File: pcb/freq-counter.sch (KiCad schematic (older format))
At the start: 63 parts, among them J1 RPM on board, J11 Hz/RPM_Terminal1, J12 Hz/RPM_Terminal0, J13 1kMG_Terminal1, J14 1kMG_Terminal0, J2 BNC, J3 RPM to Board, J4 Jack-DC, J5 Segments-Terminal0, J6 Power-Digits_Terminal0, J7 Segments-Terminal1, J8 Power-Digits_Terminal1, J9 Power-Terminal1, Q1 CSC388A, Q2 CSC388A, Q3 2SA1015, Q4 2SC1815, Q5 2SC1815, SW1 on/off, SW2 count up, SW3 toggle, SW4 SW_SIGNAL, U1 SN74HC02N, U2 ATTINY4313-PU(freq-counter), U3 EE-SX460, Y1 10MHz

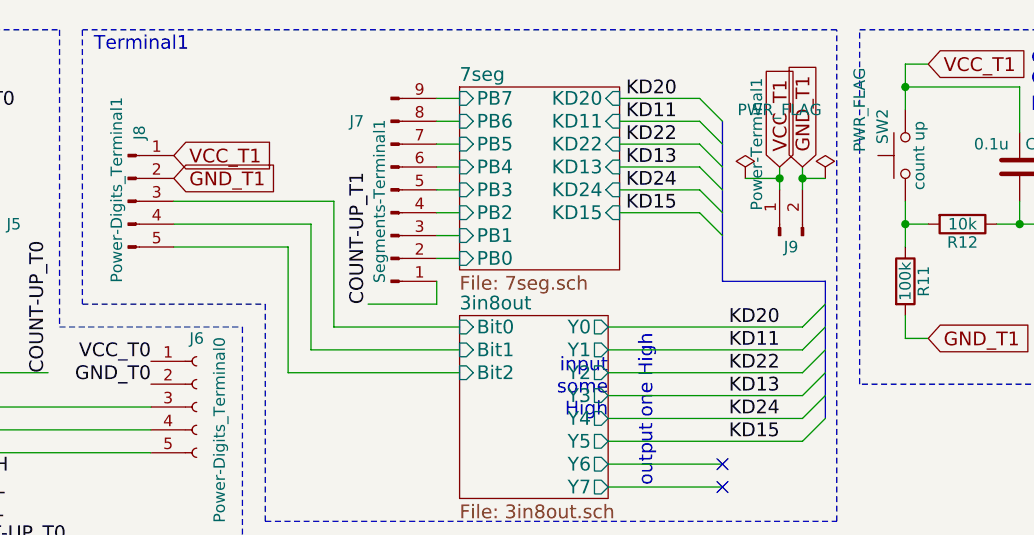
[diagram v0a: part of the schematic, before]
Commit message: ほぼ完成。電源ON/OFFの switch を slide switch に変更する必要があるけど保留。
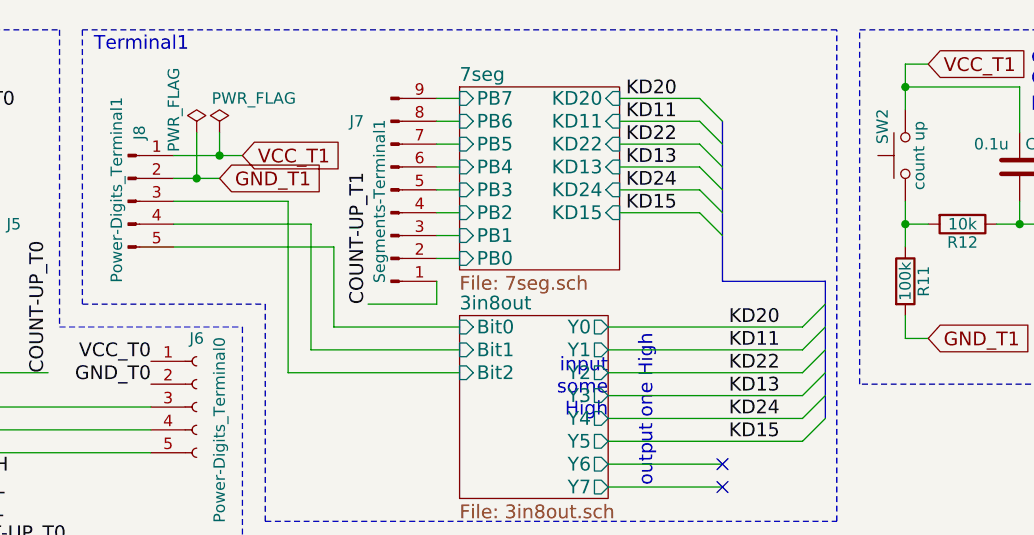
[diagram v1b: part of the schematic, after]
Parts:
- removed J9: Power-Terminal1, Conn_JST:JST_XH_B02B-XH-A_1x02_P2.50mm_Horizontal, symbol Conn_01x02_Male
- J1, J3: footprint Conn_JST:JST_XH_B03B-XH-A_1x03_P2.50mm_Horizontal -> Connector_JST:JST_XH_B03B-XH-A_1x03_P2.50mm_Horizontal
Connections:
- net 3in8out/Bit0: now also J8.5 (Pin_5); no longer J8.3 (Pin_3)
- net 3in8out/Bit2: now also J8.3 (Pin_3); no longer J8.5 (Pin_5)
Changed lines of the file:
@@
 $EndComp
 $Comp
-L GND #PWR4
+L GND #PWR01
 U 1 1 5A10C10B
 P 1450 5100
-F 0 "#PWR4" H 1450 4850 50  0001 C CNN
+F 0 "#PWR01" H 1450 4850 50  0001 C CNN
 F 1 "GND" H 1450 4950 50  0000 C CNN
 F 2 "" H 1450 5100 50  0001 C CNN
@@
 $EndComp
 $Comp
-L GND #PWR13
+L GND #PWR02
 U 1 1 5A102C86
 P 5050 6000
-F 0 "#PWR13" H 5050 5750 50  0001 C CNN
+F 0 "#PWR02" H 5050 5750 50  0001 C CNN
 F 1 "GND" H 5050 5850 50  0000 C CNN
 F 2 "" H 5050 6000 50  0001 C CNN
@@
 F 0 "J3" H 6850 5400 50  0000 C CNN
 F 1 "RPM to Board" H 6850 5000 50  0000 C CNN
-F 2 "Conn_JST:JST_XH_B03B-XH-A_1x03_P2.50mm_Horizontal" H 6850 5200 50  0001 C CNN
+F 2 "Connector_JST:JST_XH_B03B-XH-A_1x03_P2.50mm_Horizontal" H 6850 5200 50  0001 C CNN
 F 3 "" H 6850 5200 50  0001 C CNN
 	1    6850 5200
@@
 F 0 "J1" H 4750 4600 50  0000 C CNN
 F 1 "RPM on board" H 4650 4200 50  0000 C CNN
-F 2 "Conn_JST:JST_XH_B03B-XH-A_1x03_P2.50mm_Horizontal" H 4750 4400 50  0001 C CNN
+F 2 "Connector_JST:JST_XH_B03B-XH-A_1x03_P2.50mm_Horizontal" H 4750 4400 50  0001 C CNN
 F 3 "" H 4750 4400 50  0001 C CNN
 	1    4750 4400
@@
 $EndComp
 $Comp
-L GND #PWR3
+L GND #PWR03
 U 1 1 5A14ACE7
 P 1250 2200
-F 0 "#PWR3" H 1250 1950 50  0001 C CNN
+F 0 "#PWR03" H 1250 1950 50  0001 C CNN
 F 1 "GND" H 1250 2050 50  0000 C CNN
 F 2 "" H 1250 2200 50  0001 C CNN
@@
 $EndComp
 $Comp
-L PWR_FLAG #FLG1
+L PWR_FLAG #FLG04
 U 1 1 5A14B084
 P 1150 2000
-F 0 "#FLG1" H 1150 2075 50  0001 C CNN
+F 0 "#FLG04" H 1150 2075 50  0001 C CNN
 F 1 "PWR_FLAG" H 1150 2150 50  0000 C CNN
 F 2 "" H 1150 2000 50  0001 C CNN
@@
 $EndComp
 $Comp
-L PWR_FLAG #FLG2
+L PWR_FLAG #FLG05
 U 1 1 5A14B889
 P 1950 1050
-F 0 "#FLG2" H 1950 1125 50  0001 C CNN
+F 0 "#FLG05" H 1950 1125 50  0001 C CNN
 F 1 "PWR_FLAG" H 2100 1350 50  0000 C CNN
 F 2 "" H 1950 1050 50  0001 C CNN
@@
 $EndComp
 $Comp
-L GND #PWR8
+L GND #PWR06
 U 1 1 5A14CF4C
 P 2900 1700
-F 0 "#PWR8" H 2900 1450 50  0001 C CNN
+F 0 "#PWR06" H 2900 1450 50  0001 C CNN
 F 1 "GND" H 2900 1550 50  0000 C CNN
 F 2 "" H 2900 1700 50  0001 C CNN
@@
 Power
 $Comp
-L PWR_FLAG #FLG4
+L PWR_FLAG #FLG07
 U 1 1 5A15C58C
 P 5500 5050
-F 0 "#FLG4" H 5500 5125 50  0001 C CNN
+F 0 "#FLG07" H 5500 5125 50  0001 C CNN
 F 1 "PWR_FLAG" H 5450 5200 50  0000 C CNN
 F 2 "" H 5500 5050 50  0001 C CNN
@@
 $EndComp
 $Comp
-L PWR_FLAG #FLG3
+L PWR_FLAG #FLG08
 U 1 1 5A15C934
 P 5450 5400
-F 0 "#FLG3" H 5450 5475 50  0001 C CNN
+F 0 "#FLG08" H 5450 5475 50  0001 C CNN
 F 1 "PWR_FLAG" V 5350 5400 50  0000 C CNN
 F 2 "" H 5450 5400 50  0001 C CNN
@@
 NoConn ~ 1200 1150
 $Comp
-L VCC #PWR5
+L VCC #PWR09
 U 1 1 5A193502
 P 2050 1050
-F 0 "#PWR5" H 2050 900 50  0001 C CNN
+F 0 "#PWR09" H 2050 900 50  0001 C CNN
 F 1 "VCC" H 2050 1200 50  0000 C CNN
 F 2 "" H 2050 1050 50  0001 C CNN
@@
 Terminal1
 $Comp
-L Conn_01x02_Male J9
-U 1 1 5A1FF28B
-P 8800 1650
-F 0 "J9" V 8750 1600 50  0000 C CNN
-F 1 "Power-Terminal1" H 9200 1750 50  0000 C CNN
-F 2 "Conn_JST:JST_XH_B02B-XH-A_1x02_P2.50mm_Horizontal" H 8800 1650 50  0001 C CNN
-F 3 "" H 8800 1650 50  0001 C CNN
-	1    8800 1650
-	0    -1   -1   0
-$EndComp
-Text GLabel 8900 1350 1    60   Input ~ 0
-GND_T1
-$Comp
-L VCC #PWR7
+L VCC #PWR010
 U 1 1 5A20AA1B
 P 2800 1100
-F 0 "#PWR7" H 2800 950 50  0001 C CNN
+F 0 "#PWR010" H 2800 950 50  0001 C CNN
 F 1 "VCC" H 2800 1250 50  0000 C CNN
 F 2 "" H 2800 1100 50  0001 C CNN
@@
 	1    0    0    -1
 $EndComp
-Text GLabel 8800 1350 1    60   Input ~ 0
-VCC_T1
-$Comp
-L PWR_FLAG #FLG6
+$Comp
+L PWR_FLAG #FLG011
 U 1 1 5A1E7BBB
-P 9000 1400
-F 0 "#FLG6" H 9000 1475 50  0001 C CNN
-F 1 "PWR_FLAG" V 9150 1700 50  0000 C CNN
-F 2 "" H 9000 1400 50  0001 C CNN
-F 3 "" H 9000 1400 50  0001 C CNN
-	1    9000 1400
-	1    0    0    -1
-$EndComp
-$Comp
-L PWR_FLAG #FLG5
+P 6350 1200
+F 0 "#FLG011" H 6350 1275 50  0001 C CNN
+F 1 "PWR_FLAG" H 6500 1350 50  0000 C CNN
+F 2 "" H 6350 1200 50  0001 C CNN
+F 3 "" H 6350 1200 50  0001 C CNN
+	1    6350 1200
+	1    0    0    -1
+$EndComp
+$Comp
+L PWR_FLAG #FLG012
 U 1 1 5A1E8382
-P 8650 1400
-F 0 "#FLG5" H 8650 1475 50  0001 C CNN
-F 1 "PWR_FLAG" H 8800 1700 50  0000 C CNN
-F 2 "" H 8650 1400 50  0001 C CNN
-F 3 "" H 8650 1400 50  0001 C CNN
-	1    8650 1400
-	1    0    0    -1
-$EndComp
-$Comp
-L VCC #PWR2
+P 6250 1200
+F 0 "#FLG012" H 6250 1275 50  0001 C CNN
+F 1 "PWR_FLAG" V 6150 1300 50  0000 C CNN
+F 2 "" H 6250 1200 50  0001 C CNN
+F 3 "" H 6250 1200 50  0001 C CNN
+	1    6250 1200
+	1    0    0    -1
+$EndComp
+$Comp
+L VCC #PWR013
 U 1 1 5A1EAB1C
 P 1000 4500
-F 0 "#PWR2" H 1000 4350 50  0001 C CNN
+F 0 "#PWR013" H 1000 4350 50  0001 C CNN
 F 1 "VCC" H 1000 4650 50  0000 C CNN
 F 2 "" H 1000 4500 50  0001 C CNN
@@
 $EndComp
 $Comp
-L GND #PWR11
+L GND #PWR014
 U 1 1 5A1EBF20
 P 3100 3100
-F 0 "#PWR11" H 3100 2850 50  0001 C CNN
+F 0 "#PWR014" H 3100 2850 50  0001 C CNN
 F 1 "GND" H 3100 2950 50  0000 C CNN
 F 2 "" H 3100 3100 50  0001 C CNN
@@
 $EndComp
 $Comp
-L GND #PWR6
+L GND #PWR015
 U 1 1 5A1ECBC1
 P 2450 6400
-F 0 "#PWR6" H 2450 6150 50  0001 C CNN
+F 0 "#PWR015" H 2450 6150 50  0001 C CNN
 F 1 "GND" H 2450 6250 50  0000 C CNN
 F 2 "" H 2450 6400 50  0001 C CNN
@@
 $EndComp
 $Comp
-L GND #PWR1
+L GND #PWR016
 U 1 1 5A1ED93F
 P 850 4550
-F 0 "#PWR1" H 850 4300 50  0001 C CNN
+F 0 "#PWR016" H 850 4300 50  0001 C CNN
 F 1 "GND" H 850 4400 50  0000 C CNN
 F 2 "" H 850 4550 50  0001 C CNN
@@
 $EndComp
 $Comp
-L GND #PWR10
+L GND #PWR017
 U 1 1 5A1EE509
 P 2950 4800
-F 0 "#PWR10" H 2950 4550 50  0001 C CNN
+F 0 "#PWR017" H 2950 4550 50  0001 C CNN
 F 1 "GND" H 2950 4650 50  0000 C CNN
 F 2 "" H 2950 4800 50  0001 C CNN
@@
 $EndComp
 $Comp
-L VCC #PWR12
+L VCC #PWR018
 U 1 1 5A1EEDD1
 P 3100 5250
-F 0 "#PWR12" H 3100 5100 50  0001 C CNN
+F 0 "#PWR018" H 3100 5100 50  0001 C CNN
 F 1 "VCC" H 3100 5400 50  0000 C CNN
 F 2 "" H 3100 5250 50  0001 C CNN
@@
 $EndComp
 $Comp
-L VCC #PWR9
+L VCC #PWR019
 U 1 1 5A1EFB20
 P 2950 3700
-F 0 "#PWR9" H 2950 3550 50  0001 C CNN
+F 0 "#PWR019" H 2950 3550 50  0001 C CNN
 F 1 "VCC" H 2950 3850 50  0000 C CNN
 F 2 "" H 2950 3700 50  0001 C CNN
@@
 $EndComp
 $Comp
-L GND #PWR17
+L GND #PWR020
 U 1 1 5A1F0879
 P 7900 6150
-F 0 "#PWR17" H 7900 5900 50  0001 C CNN
+F 0 "#PWR020" H 7900 5900 50  0001 C CNN
 F 1 "GND" H 7900 6000 50  0000 C CNN
 F 2 "" H 7900 6150 50  0001 C CNN
@@
 $EndComp
 $Comp
-L VCC #PWR16
+L VCC #PWR021
 U 1 1 5A1F0C13
 P 7900 3850
-F 0 "#PWR16" H 7900 3700 50  0001 C CNN
+F 0 "#PWR021" H 7900 3700 50  0001 C CNN
 F 1 "VCC" H 7900 4000 50  0000 C CNN
 F 2 "" H 7900 3850 50  0001 C CNN
@@
 $EndComp
 $Comp
-L GND #PWR15
+L GND #PWR022
 U 1 1 5A1F3CDE
 P 6350 3650
-F 0 "#PWR15" H 6350 3400 50  0001 C CNN
+F 0 "#PWR022" H 6350 3400 50  0001 C CNN
 F 1 "GND" H 6350 3500 50  0000 C CNN
 F 2 "" H 6350 3650 50  0001 C CNN
@@
 $EndComp
 $Comp
-L VCC #PWR14
+L VCC #PWR023
 U 1 1 5A1F4C25
 P 5800 4400
-F 0 "#PWR14" H 5800 4250 50  0001 C CNN
+F 0 "#PWR023" H 5800 4250 50  0001 C CNN
 F 1 "VCC" H 5800 4550 50  0000 C CNN
 F 2 "" H 5800 4400 50  0001 C CNN
@@
 	5000 2700 5100 2700
 Wire Wire Line
-	6650 2250 7400 2250
-Wire Wire Line
-	6850 2050 7400 2050
-Wire Wire Line
-	6750 2150 7400 2150
-Wire Wire Line
 	7300 1750 7400 1750
 Wire Wire Line
@@
 	9050 750  5750 750
 Wire Wire Line
-	8800 1350 8800 1450
-Wire Wire Line
-	8900 1350 8900 1450
-Wire Wire Line
 	2050 1500 2000 1500
 Wire Wire Line
@@
 Wire Wire Line
 	1850 1150 2050 1150
-Wire Wire Line
-	9000 1400 8900 1400
-Connection ~ 8900 1400
-Wire Wire Line
-	8650 1400 8800 1400
-Connection ~ 8800 1400
 Wire Wire Line
 	3100 3100 3100 3000
@@
 	1    0    0    -1
 $EndComp
-Text GLabel 6150 1300 2    60   Input ~ 0
+Text GLabel 6450 1300 2    60   Input ~ 0
 VCC_T1
-Text GLabel 6150 1400 2    60   Input ~ 0
+Text GLabel 6350 1400 2    60   Input ~ 0
 GND_T1
 Wire Wire Line
-	6150 1500 6850 1500
-Wire Wire Line
-	6850 1500 6850 2050
+	6150 1500 6650 1500
+Wire Wire Line
+	6650 1500 6650 2250
 Wire Wire Line
 	6150 1600 6750 1600
@@
 	6750 1600 6750 2150
 Wire Wire Line
-	6650 2250 6650 1700
-Wire Wire Line
-	6650 1700 6150 1700
+	6850 1700 6150 1700
 Wire Notes Line
 	5750 750  5750 1950
@@
 Wire Notes Line
 	6550 1950 6550 2900
+Wire Wire Line
+	6750 2150 7400 2150
+Wire Wire Line
+	6650 2250 7400 2250
+Wire Wire Line
+	6850 1700 6850 2050
+Wire Wire Line
+	6850 2050 7400 2050
+Wire Wire Line
+	6350 1400 6150 1400
+Wire Wire Line
+	6150 1300 6450 1300
+Wire Wire Line
+	6250 1200 6250 1400
+Connection ~ 6250 1400
+Wire Wire Line
+	6350 1200 6350 1300
+Connection ~ 6350 1300
 $EndSCHEMATC

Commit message: Power ON/OFF switch を slide switch に変更。
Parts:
- SW1: footprint freq-counter:SW_Toggle_x1 -> freq-counter:SS12D01G4
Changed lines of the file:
@@
 F 0 "SW1" H 1650 1420 50  0000 C CNN
 F 1 "on/off" H 1650 1500 50  0000 C CNN
-F 2 "freq-counter:SW_Toggle_x1" H 1650 1250 50  0001 C CNN
+F 2 "freq-counter:SS12D01G4" H 1650 1250 50  0001 C CNN
 F 3 "" H 1650 1250 50  0001 C CNN
 	1    1650 1250

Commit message: RPM on board を PinHeaderに変更。
手持ちの部品にJST_XH_B03B-XH-A_1x03_P2.50mmの横向きがなかったため。
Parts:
- J1: footprint Connector_JST:JST_XH_B03B-XH-A_1x03_P2.50mm_Horizontal -> Connector_PinHeader_2.54mm:PinHeader_1x03_P2.54mm_Horizontal
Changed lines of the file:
@@
 F 0 "J1" H 4750 4600 50  0000 C CNN
 F 1 "RPM on board" H 4650 4200 50  0000 C CNN
-F 2 "Connector_JST:JST_XH_B03B-XH-A_1x03_P2.50mm_Horizontal" H 4750 4400 50  0001 C CNN
+F 2 "Connector_PinHeader_2.54mm:PinHeader_1x03_P2.54mm_Horizontal" H 4750 4400 50  0001 C CNN
 F 3 "" H 4750 4400 50  0001 C CNN
 	1    4750 4400

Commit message: ON/OFF の slide switch を横型に変更。
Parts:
- SW1: footprint freq-counter:SS12D01G4 -> freq-counter:SK-12D01-VG4
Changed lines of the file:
@@
 F 0 "SW1" H 1650 1420 50  0000 C CNN
 F 1 "on/off" H 1650 1500 50  0000 C CNN
-F 2 "freq-counter:SS12D01G4" H 1650 1250 50  0001 C CNN
+F 2 "freq-counter:SK-12D01-VG4" H 1650 1250 50  0001 C CNN
 F 3 "" H 1650 1250 50  0001 C CNN
 	1    1650 1250

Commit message: Power ON/OFF の slide switch を横型から縦型に変更。
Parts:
- SW1: footprint freq-counter:SK-12D01-VG4 -> freq-counter:SS12D01G4
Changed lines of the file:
@@
 F 0 "SW1" H 1650 1420 50  0000 C CNN
 F 1 "on/off" H 1650 1500 50  0000 C CNN
-F 2 "freq-counter:SK-12D01-VG4" H 1650 1250 50  0001 C CNN
+F 2 "freq-counter:SS12D01G4" H 1650 1250 50  0001 C CNN
 F 3 "" H 1650 1250 50  0001 C CNN
 	1    1650 1250

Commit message: 3Dpackages が表示されるように，旧式の3D modelを使うようにした。
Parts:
- C1, C3, C7: footprint Capacitors_THT:CP_Radial_D5.0mm_P2.50mm -> Capacitor_THT:CP_Radial_D5.0mm_P2.50mm
- C2, C4, C8, C9: footprint Capacitors_THT:C_Disc_D3.4mm_W2.1mm_P2.50mm -> Capacitor_THT:C_Disc_D3.0mm_W1.6mm_P2.50mm
- C5, C6: footprint Capacitors_THT:C_Disc_D3.0mm_W1.6mm_P2.50mm -> Capacitor_THT:C_Disc_D3.0mm_W1.6mm_P2.50mm
- Q1, Q2, Q3, Q4, Q5: footprint Package_TO_SOT_THT:TO-92_Inline_Wide -> TO_SOT_Packages_THT:TO-92_Inline_Wide
- U1: footprint Housings_DIP:DIP-14_W7.62mm -> Package_DIP:DIP-14_W7.62mm
- U2: footprint Housings_DIP:DIP-20_W7.62mm -> Package_DIP:DIP-20_W7.62mm
- Y1: footprint Crystals:Crystal_HC49-4H_Vertical -> Crystal:Crystal_HC49-4H_Vertical
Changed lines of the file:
@@
 F 0 "Q2" H 3400 6175 50  0000 L CNN
 F 1 "CSC388A" H 3400 6100 50  0000 L CNN
-F 2 "Package_TO_SOT_THT:TO-92_Inline_Wide" H 3400 6025 50  0001 L CIN
+F 2 "TO_SOT_Packages_THT:TO-92_Inline_Wide" H 3400 6025 50  0001 L CIN
 F 3 "" H 3200 6100 50  0001 L CNN
 	1    3200 6100
@@
 F 0 "Q1" H 3000 4650 50  0000 L CNN
 F 1 "CSC388A" V 3250 4350 50  0000 L CNN
-F 2 "Package_TO_SOT_THT:TO-92_Inline_Wide" H 3250 4425 50  0001 L CIN
+F 2 "TO_SOT_Packages_THT:TO-92_Inline_Wide" H 3250 4425 50  0001 L CIN
 F 3 "" H 3050 4500 50  0001 L CNN
 	1    3050 4500
@@
 F 0 "C8" H 9875 1450 50  0000 L CNN
 F 1 "0.1u" H 9650 1450 50  0000 L CNN
-F 2 "Capacitors_THT:C_Disc_D3.4mm_W2.1mm_P2.50mm" H 9888 1200 50  0001 C CNN
+F 2 "Capacitor_THT:C_Disc_D3.0mm_W1.6mm_P2.50mm" H 9888 1200 50  0001 C CNN
 F 3 "" H 9850 1350 50  0001 C CNN
 	1    9850 1350
@@
 F 0 "U2" H 3250 3050 50  0000 C CNN
 F 1 "ATTINY4313-PU(freq-counter)" H 4100 3050 50  0000 C CNN
-F 2 "Housings_DIP:DIP-20_W7.62mm" V 3650 2050 50  0001 C CIN
+F 2 "Package_DIP:DIP-20_W7.62mm" V 3650 2050 50  0001 C CIN
 F 3 "" H 3650 2050 50  0001 C CNN
 	1    4100 2000
@@
 F 0 "Q5" H 10000 5250 50  0000 L CNN
 F 1 "2SC1815" V 10350 5050 50  0000 L CNN
-F 2 "Package_TO_SOT_THT:TO-92_Inline_Wide" H 10350 5125 50  0001 L CIN
+F 2 "TO_SOT_Packages_THT:TO-92_Inline_Wide" H 10350 5125 50  0001 L CIN
 F 3 "" H 10150 5200 50  0001 L CNN
 	1    10150 5200
@@
 F 0 "Q4" H 8800 5300 50  0000 L CNN
 F 1 "2SC1815" V 9100 5000 50  0000 L CNN
-F 2 "Package_TO_SOT_THT:TO-92_Inline_Wide" H 9100 5075 50  0001 L CIN
+F 2 "TO_SOT_Packages_THT:TO-92_Inline_Wide" H 9100 5075 50  0001 L CIN
 F 3 "" H 8900 5150 50  0001 L CNN
 	1    8900 5150
@@
 F 0 "Q3" V 8950 4150 50  0000 L CNN
 F 1 "2SA1015" V 9050 4100 50  0000 L CNN
-F 2 "Package_TO_SOT_THT:TO-92_Inline_Wide" H 9000 3975 50  0001 L CIN
+F 2 "TO_SOT_Packages_THT:TO-92_Inline_Wide" H 9000 3975 50  0001 L CIN
 F 3 "" H 8800 4050 50  0001 L CNN
 	1    8800 4050
@@
 F 0 "C9" H 9750 5900 50  0000 L CNN
 F 1 "0.1u" H 9750 5700 50  0000 L CNN
-F 2 "Capacitors_THT:C_Disc_D3.4mm_W2.1mm_P2.50mm" H 9888 5650 50  0001 C CNN
+F 2 "Capacitor_THT:C_Disc_D3.0mm_W1.6mm_P2.50mm" H 9888 5650 50  0001 C CNN
 F 3 "" H 9850 5800 50  0001 C CNN
 	1    9850 5800
@@
 F 0 "C7" H 8225 5900 50  0000 L CNN
 F 1 "4.7u" H 8225 5700 50  0000 L CNN
-F 2 "Capacitors_THT:CP_Radial_D5.0mm_P2.50mm" H 8238 5650 50  0001 C CNN
+F 2 "Capacitor_THT:CP_Radial_D5.0mm_P2.50mm" H 8238 5650 50  0001 C CNN
 F 3 "" H 8200 5800 50  0001 C CNN
 	1    8200 5800
@@
 F 0 "U1" H 1800 4750 60  0000 C CNN
 F 1 "SN74HC02N" H 2300 5100 60  0000 C CNN
-F 2 "Housings_DIP:DIP-14_W7.62mm" H 2500 5100 60  0001 C CNN
+F 2 "Package_DIP:DIP-14_W7.62mm" H 2500 5100 60  0001 C CNN
 F 3 "" H 2500 5100 60  0001 C CNN
 	1    2250 5000
@@
 F 0 "C1" H 1475 4850 50  0000 L CNN
 F 1 "100u" V 1400 4500 50  0000 L CNN
-F 2 "Capacitors_THT:CP_Radial_D5.0mm_P2.50mm" H 1488 4600 50  0001 C CNN
+F 2 "Capacitor_THT:CP_Radial_D5.0mm_P2.50mm" H 1488 4600 50  0001 C CNN
 F 3 "" H 1450 4750 50  0001 C CNN
 	1    1450 4750
@@
 F 0 "C2" H 1675 4850 50  0000 L CNN
 F 1 "0.1u" H 1675 4650 50  0000 L CNN
-F 2 "Capacitors_THT:C_Disc_D3.4mm_W2.1mm_P2.50mm" H 1688 4600 50  0001 C CNN
+F 2 "Capacitor_THT:C_Disc_D3.0mm_W1.6mm_P2.50mm" H 1688 4600 50  0001 C CNN
 F 3 "" H 1650 4750 50  0001 C CNN
 	1    1650 4750
@@
 F 0 "C5" H 4750 6150 50  0000 L CNN
 F 1 "22p" H 4700 5950 50  0000 L CNN
-F 2 "Capacitors_THT:C_Disc_D3.0mm_W1.6mm_P2.50mm" H 4888 5900 50  0001 C CNN
+F 2 "Capacitor_THT:C_Disc_D3.0mm_W1.6mm_P2.50mm" H 4888 5900 50  0001 C CNN
 F 3 "" H 4850 6050 50  0001 C CNN
 	1    4850 6050
@@
 F 0 "C6" H 5275 6150 50  0000 L CNN
 F 1 "22p" H 5275 5950 50  0000 L CNN
-F 2 "Capacitors_THT:C_Disc_D3.0mm_W1.6mm_P2.50mm" H 5288 5900 50  0001 C CNN
+F 2 "Capacitor_THT:C_Disc_D3.0mm_W1.6mm_P2.50mm" H 5288 5900 50  0001 C CNN
 F 3 "" H 5250 6050 50  0001 C CNN
 	1    5250 6050
@@
 F 0 "Y1" H 5050 6550 50  0000 C CNN
 F 1 "10MHz" H 5050 6250 50  0000 C CNN
-F 2 "Crystals:Crystal_HC49-4H_Vertical" H 5050 6400 50  0001 C CNN
+F 2 "Crystal:Crystal_HC49-4H_Vertical" H 5050 6400 50  0001 C CNN
 F 3 "" H 5050 6400 50  0001 C CNN
 	1    5050 6400
@@
 F 0 "C3" H 2925 1450 50  0000 L CNN
 F 1 "100u" V 2850 1100 50  0000 L CNN
-F 2 "Capacitors_THT:CP_Radial_D5.0mm_P2.50mm" H 2938 1200 50  0001 C CNN
+F 2 "Capacitor_THT:CP_Radial_D5.0mm_P2.50mm" H 2938 1200 50  0001 C CNN
 F 3 "" H 2900 1350 50  0001 C CNN
 	1    2900 1350
@@
 F 0 "C4" H 3125 1450 50  0000 L CNN
 F 1 "0.1u" H 3125 1250 50  0000 L CNN
-F 2 "Capacitors_THT:C_Disc_D3.4mm_W2.1mm_P2.50mm" H 3138 1200 50  0001 C CNN
+F 2 "Capacitor_THT:C_Disc_D3.0mm_W1.6mm_P2.50mm" H 3138 1200 50  0001 C CNN
 F 3 "" H 3100 1350 50  0001 C CNN
 	1    3100 1350

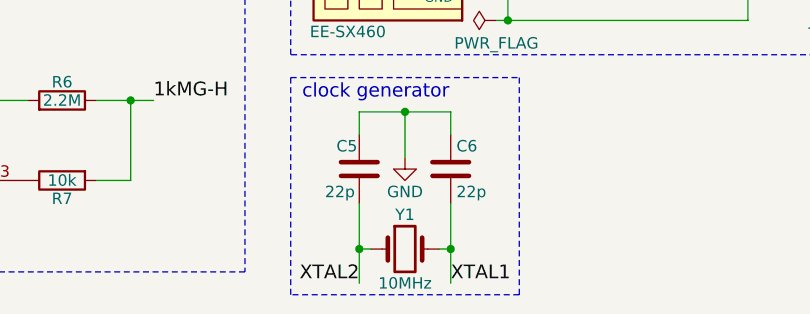
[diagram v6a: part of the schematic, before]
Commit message: clock(Y1) を 20MHz とした。
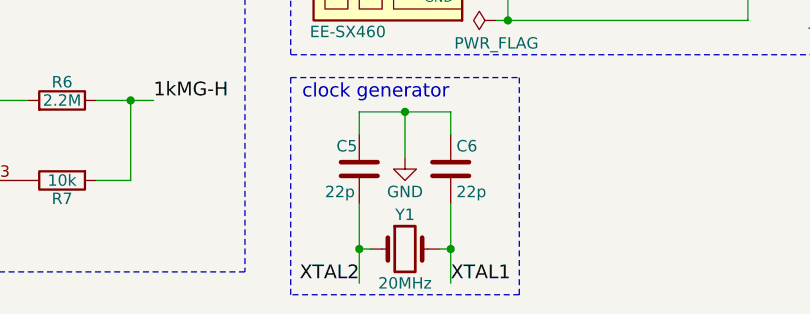
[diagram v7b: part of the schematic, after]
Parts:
- Y1: value 10MHz -> 20MHz
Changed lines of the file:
@@
 P 5050 6400
 F 0 "Y1" H 5050 6550 50  0000 C CNN
-F 1 "10MHz" H 5050 6250 50  0000 C CNN
+F 1 "20MHz" H 5050 6250 50  0000 C CNN
 F 2 "Crystal:Crystal_HC49-4H_Vertical" H 5050 6400 50  0001 C CNN
 F 3 "" H 5050 6400 50  0001 C CNN

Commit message: 忘れ物。
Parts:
- J3: footprint Connector_JST:JST_XH_B03B-XH-A_1x03_P2.50mm_Horizontal -> Connectors_JST:JST_XH_B03B-XH-A_03x2.50mm_Straight
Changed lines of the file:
@@
 F 0 "J3" H 6850 5400 50  0000 C CNN
 F 1 "RPM to Board" H 6850 5000 50  0000 C CNN
-F 2 "Connector_JST:JST_XH_B03B-XH-A_1x03_P2.50mm_Horizontal" H 6850 5200 50  0001 C CNN
+F 2 "Connectors_JST:JST_XH_B03B-XH-A_03x2.50mm_Straight" H 6850 5200 50  0001 C CNN
 F 3 "" H 6850 5200 50  0001 C CNN
 	1    6850 5200
